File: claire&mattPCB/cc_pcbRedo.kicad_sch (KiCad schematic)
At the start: 91 parts, among them J1 Conn_02x05_Odd_Even, J2 Micro_SD_Card_Det_Hirose_DM3AT, J3 4x4 Keypad, J4 DC-DC_JUMPER, J5 PS_WIRES, J6 PS_BJ, J7 DC-DC Converter, SW1 SW_Push, U1 ESP8266, U2 7in_display_controller, U3 RFID_Scanner, U4 TFT_2.8IN_DISPLAY, U5 74HC14, U6 STM32F091RCTx, U7 MEZD71201AF, U8 TPS56325x, U9 4N28

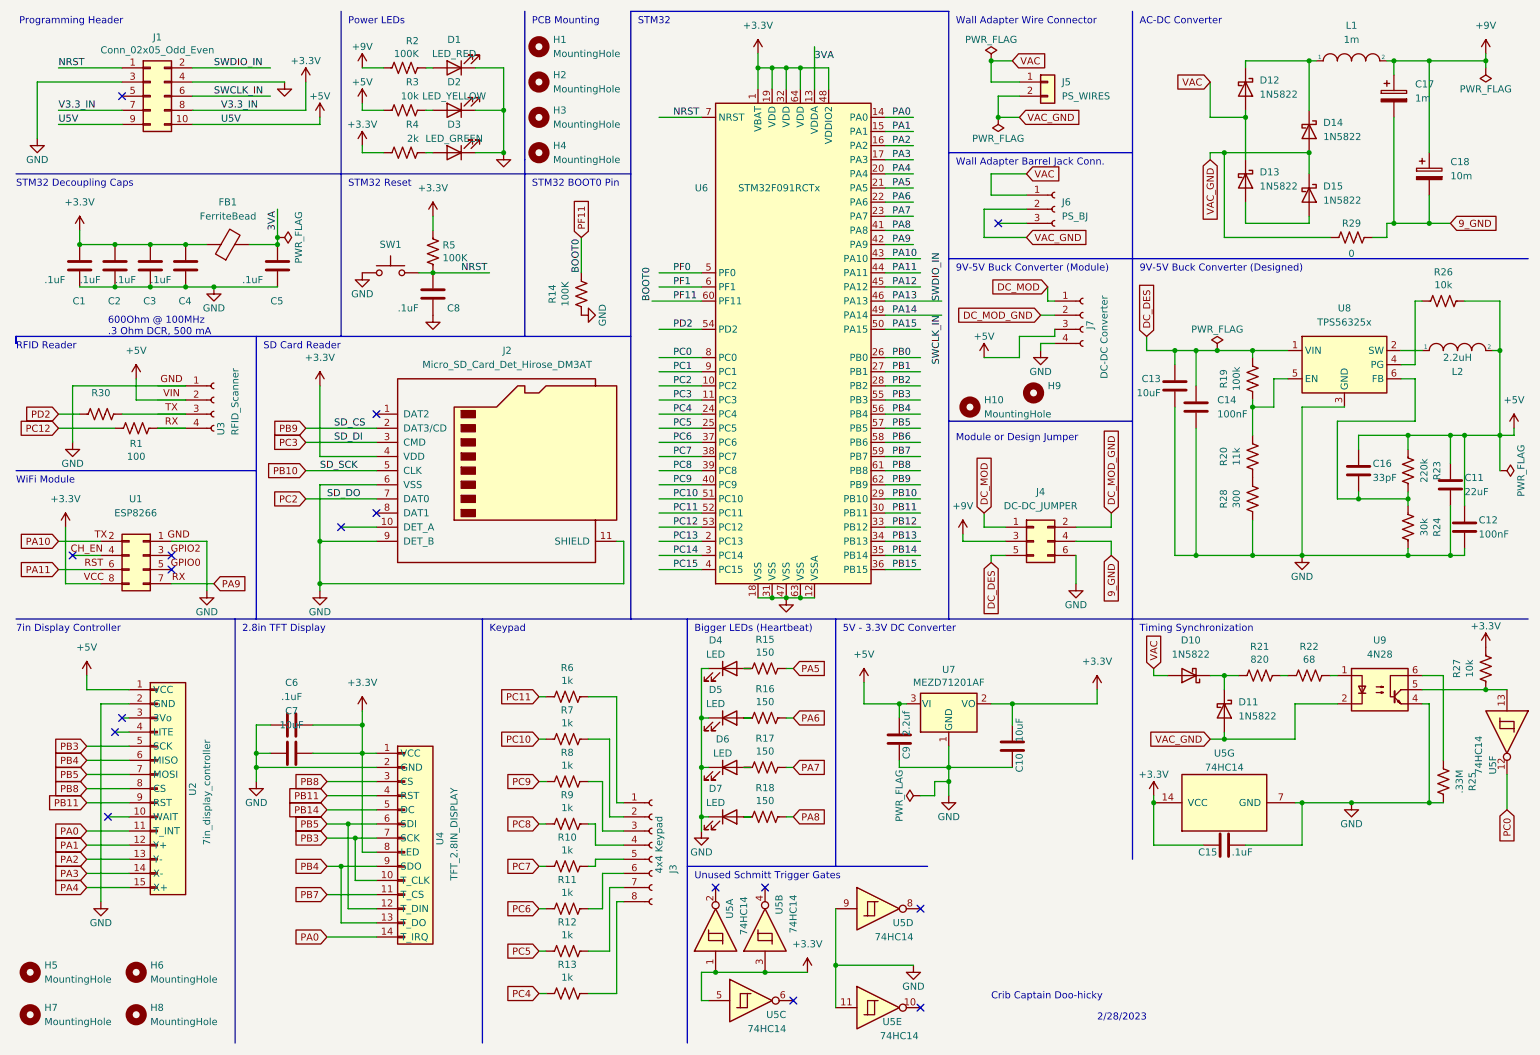
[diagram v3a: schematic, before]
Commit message: added oscillator for micro
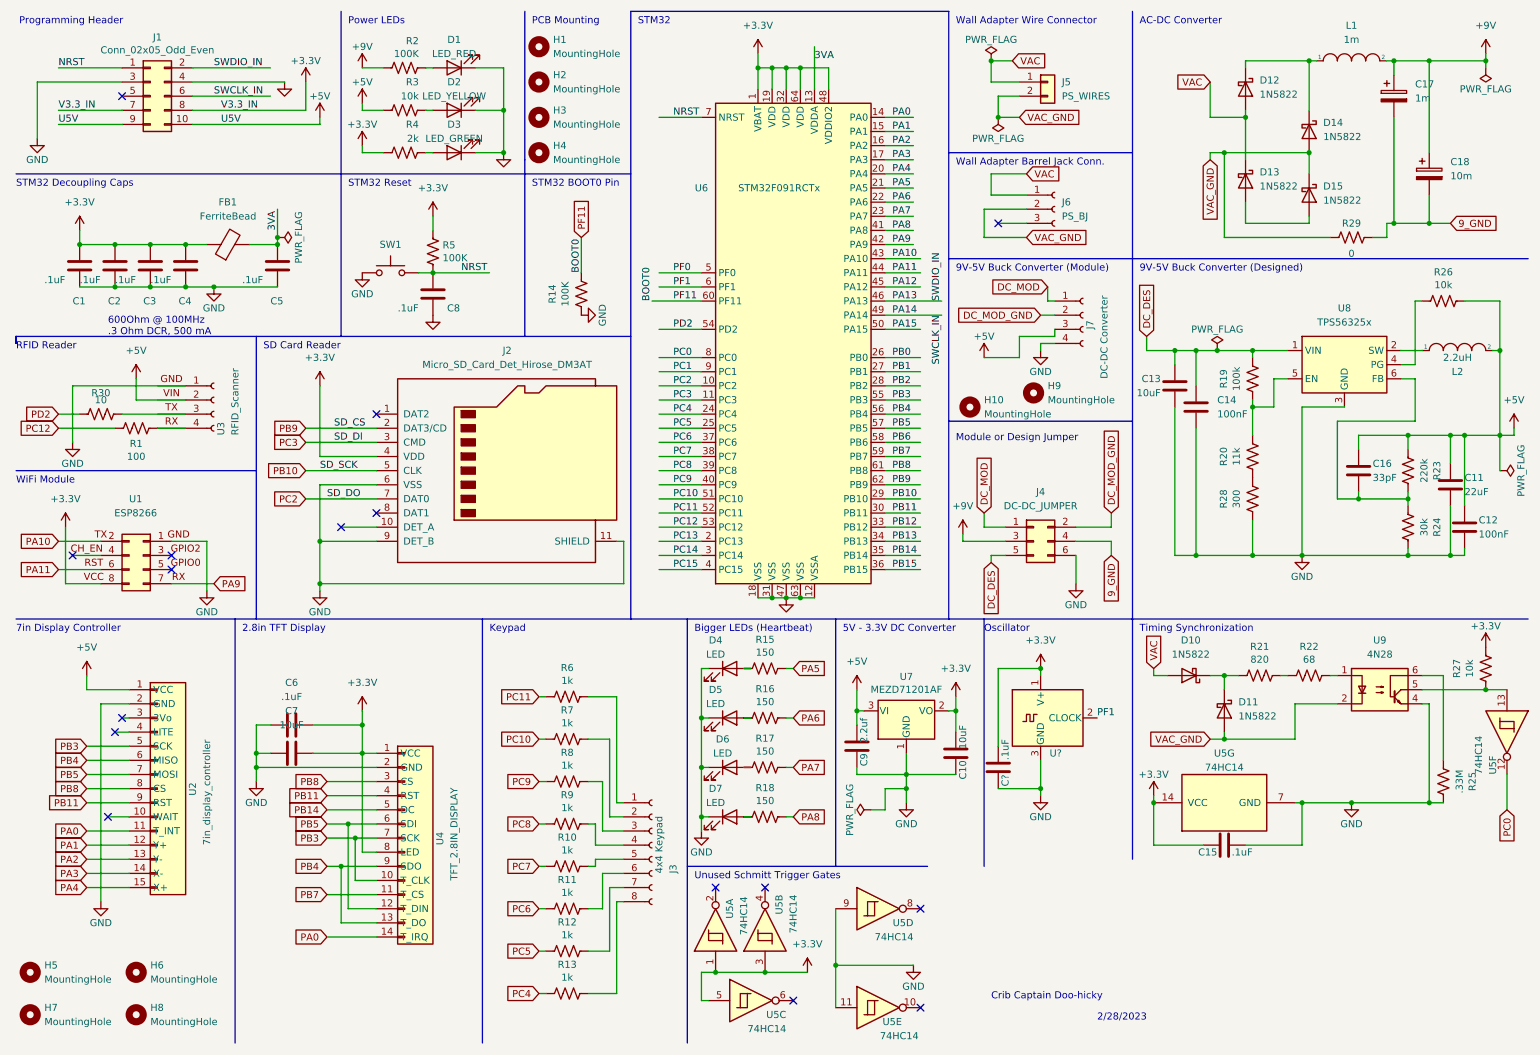
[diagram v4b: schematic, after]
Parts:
- added C?: .1uF, Capacitor_SMD:C_0805_2012Metric_Pad1.18x1.45mm_HandSolder, symbol Device:C
- added U?: (no value), symbol Oscillator:MAX7375AXR805
- H9: value (none) -> MountingHole; footprint (none) -> imported_footprints:MountingHole_2.2mm
- R30: value (none) -> 10
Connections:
- net +3V3: now also C?.2, U?.1 (V+)
- net GND: now also C?.1, U?.3 (GND)
- net PF1: now also U?.2 (CLOCK)
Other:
- note added: "Oscillator"
- moved on the sheet: C10, C9, U7

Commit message: added diodes pointing to where 5V outputs
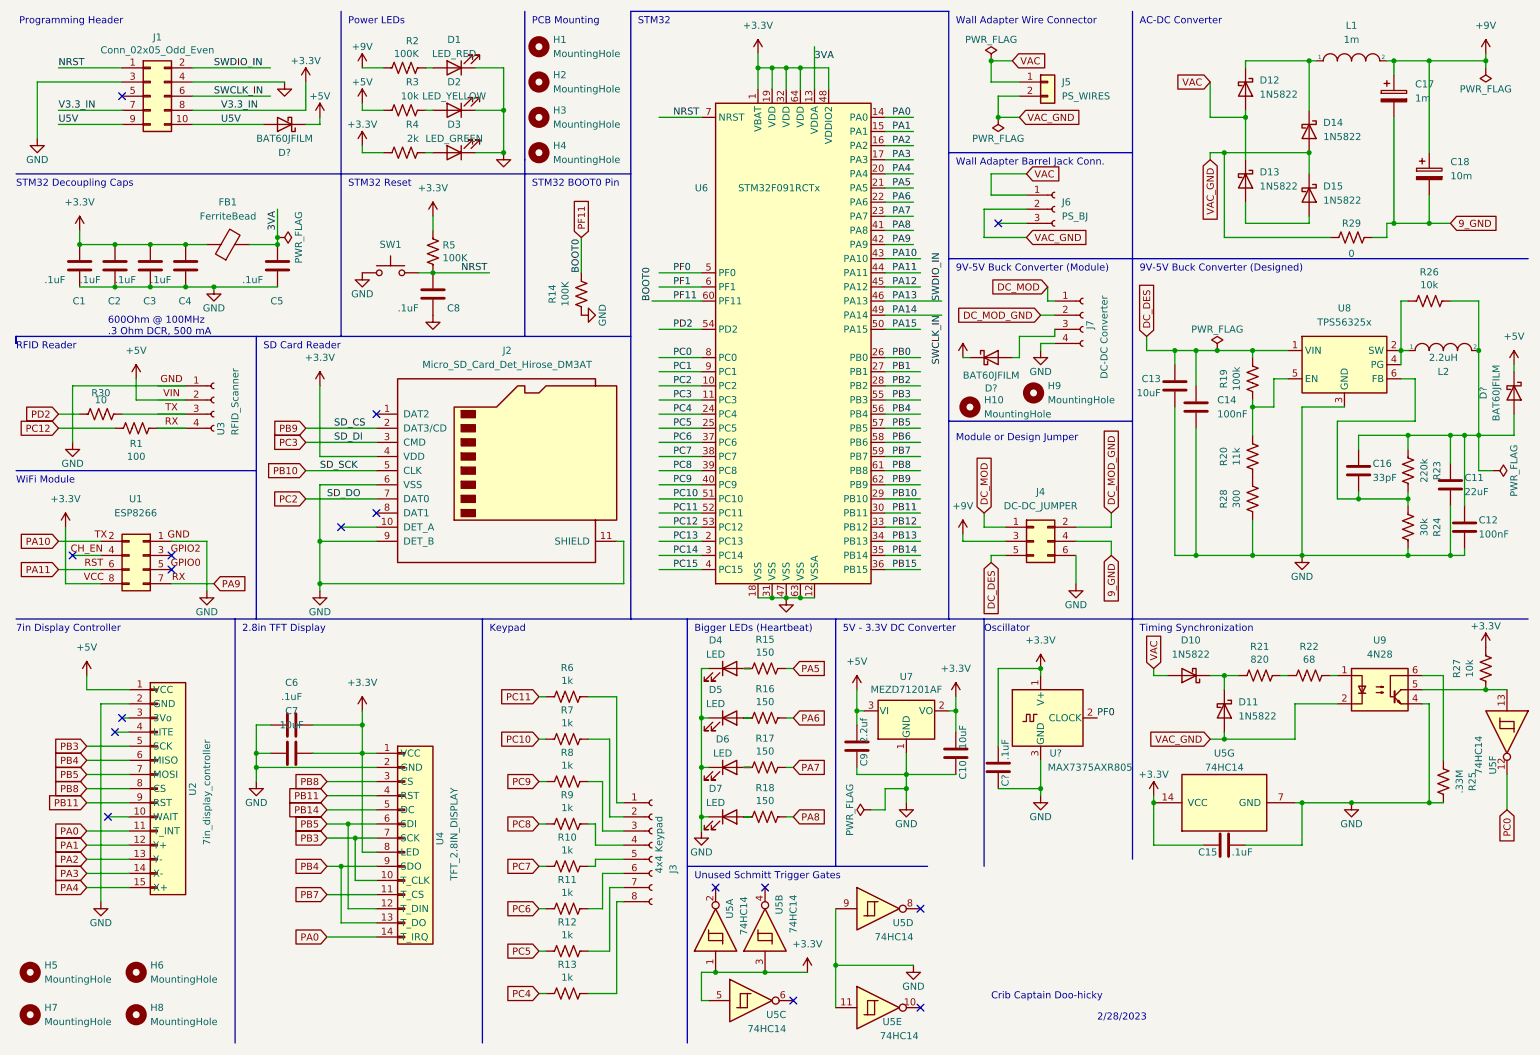
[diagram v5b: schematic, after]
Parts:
- added D? (x3): BAT60JFILM, Diode_SMD:D_SOD-323, symbol Diode:BAT60A
- U?: value (none) -> MAX7375AXR805; footprint (none) -> Package_TO_SOT_SMD:SOT-323_SC-70
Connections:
- net +5V: now also D?.1 (K), D?.1 (K), D?.1 (K); no longer C11.1, C12.1, C16.1, J1.10 (Pin_10), J1.9 (Pin_9), J7.3 (Pin_3), L2.2, R23.2, R26.1
- net PF0: now also U?.2 (CLOCK)
- net PF1: no longer U?.2 (CLOCK)
- net at R26.2, U8.4 (PG): now also L2.1, U8.2 (SW)
- new net: C11.1, C12.1, C16.1, D?.2 (A), L2.2, R23.2, R26.1
- new net: D?.2 (A), J7.3 (Pin_3)
- new net U5V: D?.2 (A), J1.10 (Pin_10), J1.9 (Pin_9)
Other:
- moved on the sheet: L2, R26

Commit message: diodes and vias w labels added
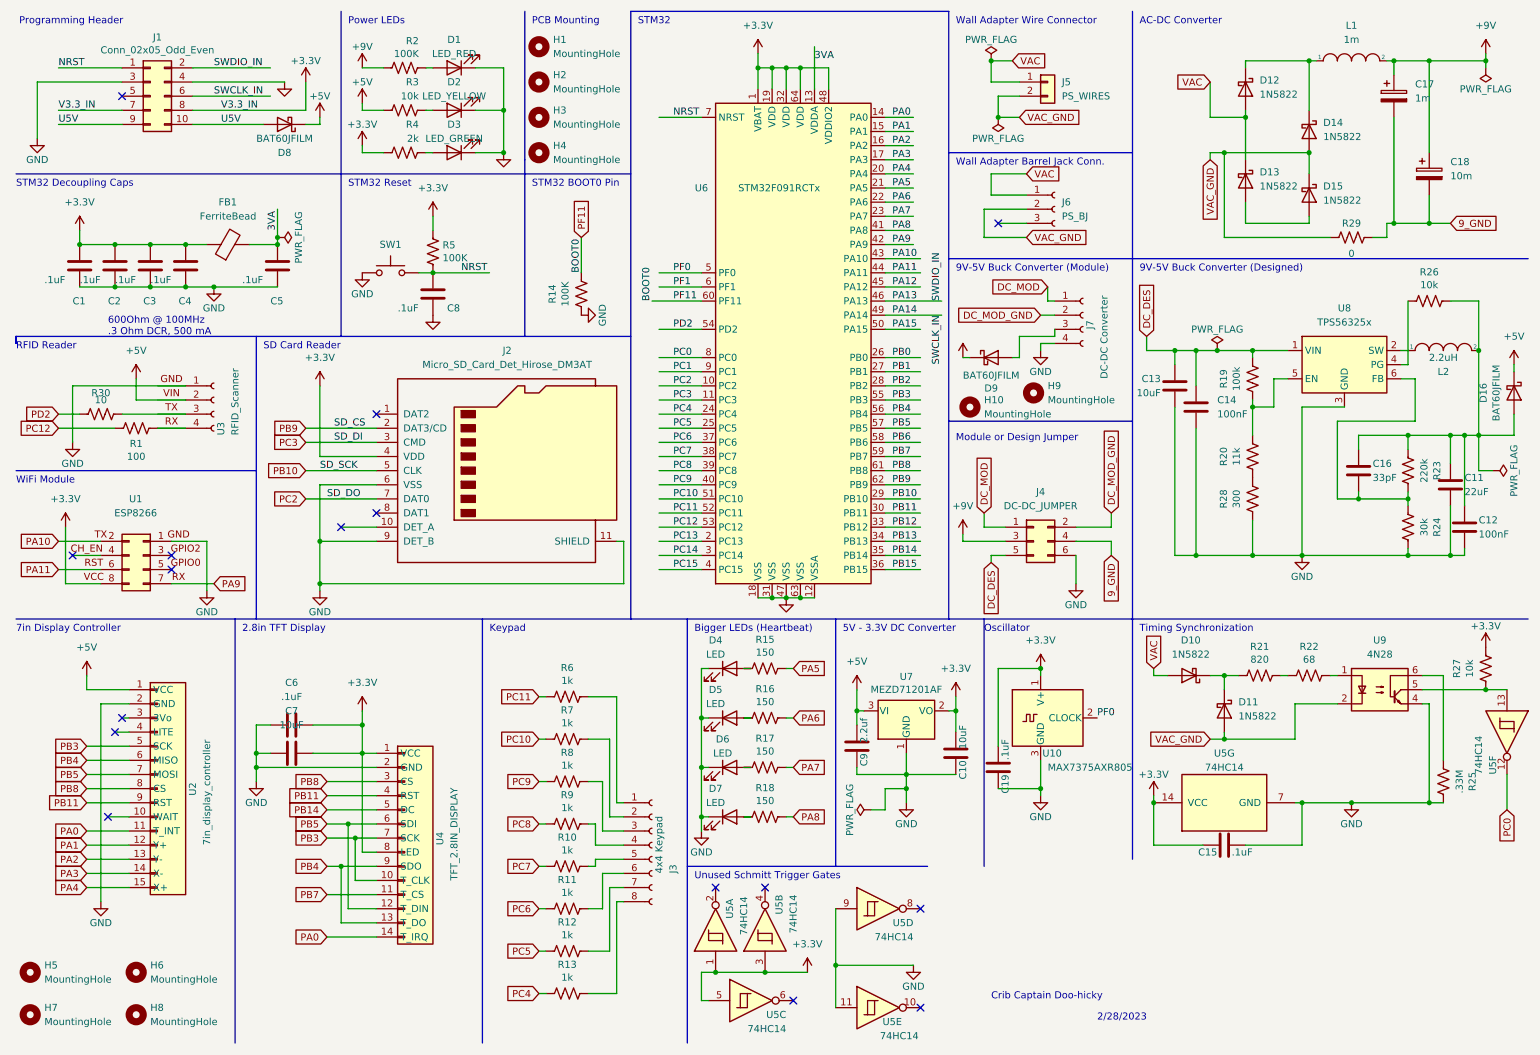
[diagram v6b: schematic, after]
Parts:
- gave numbers to parts that had none: 5
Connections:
- net at R26.2, U8.4 (PG): no longer L2.1, U8.2 (SW)
- new net: L2.1, U8.2 (SW)
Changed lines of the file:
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@@
   (junction (at 196.85 130.81) (diameter 0) (color 0 0 0 0)
   )
-  (junction (at 261.62 73.66) (diameter 0) (color 0 0 0 0)
-  )
   (junction (at 148.59 118.11) (diameter 0) (color 0 0 0 0)
   )
@@
     (stroke (width 0) (type default) (color 0 0 0 0))
   )
+  (wire (pts (xy 262.89 76.2) (xy 261.62 76.2))
+    (stroke (width 0) (type default) (color 0 0 0 0))
+  )
   (wire (pts (xy 276.86 21.59) (xy 276.86 20.32))
     (stroke (width 0) (type default) (color 0 0 0 0))
@@
     (stroke (width 0) (type default) (color 0 0 0 0))
   )
-  (wire (pts (xy 261.62 76.2) (xy 261.62 73.66))
-    (stroke (width 0) (type default) (color 0 0 0 0))
-  )
   (wire (pts (xy 144.78 130.81) (xy 143.51 130.81))
     (stroke (width 0) (type default) (color 0 0 0 0))
@@
     (stroke (width 0) (type default) (color 0 0 0 0))
   )
-  (wire (pts (xy 261.62 73.66) (xy 261.62 64.77))
-    (stroke (width 0) (type default) (color 0 0 0 0))
-  )
   (wire (pts (xy 64.77 25.4) (xy 64.77 30.48))
     (stroke (width 0) (type default) (color 0 0 0 0))
@@
     (stroke (width 0) (type default) (color 0 0 0 0))
   )
+  (wire (pts (xy 262.89 73.66) (xy 261.62 73.66))
+    (stroke (width 0) (type default) (color 0 0 0 0))
+  )
   (wire (pts (xy 266.7 50.8) (xy 266.7 45.72))
     (stroke (width 0) (type default) (color 0 0 0 0))
@@
     (stroke (width 0) (type default) (color 0 0 0 0))
   )
-  (wire (pts (xy 261.62 73.66) (xy 262.89 73.66))
-    (stroke (width 0) (type default) (color 0 0 0 0))
-  )
   (wire (pts (xy 120.65 107.95) (xy 121.92 107.95))
     (stroke (width 0) (type default) (color 0 0 0 0))
@@
     (stroke (width 0) (type default) (color 0 0 0 0))
   )
-  (wire (pts (xy 261.62 64.77) (xy 262.89 64.77))
-    (stroke (width 0) (type default) (color 0 0 0 0))
-  )
   (wire (pts (xy 68.58 179.07) (xy 77.47 179.07))
     (stroke (width 0) (type default) (color 0 0 0 0))
@@
     (stroke (width 0) (type default) (color 0 0 0 0))
   )
+  (wire (pts (xy 262.89 64.77) (xy 262.89 76.2))
+    (stroke (width 0) (type default) (color 0 0 0 0))
+  )
   (wire (pts (xy 259.08 50.8) (xy 259.08 53.34))
     (stroke (width 0) (type default) (color 0 0 0 0))
@@
   (symbol (lib_id "Oscillator:MAX7375AXR805") (at 196.85 139.7 0) (unit 1)
     (in_bom yes) (on_board yes)
-    (property "Reference" "U?" (id 0) (at 200.66 146.05 0)
+    (property "Reference" "U10" (id 0) (at 200.66 146.05 0)
       (effects (font (size 1.27 1.27)) (justify right))
     )
@@
   (symbol (lib_id "Diode:BAT60A") (at 60.96 33.02 180) (unit 1)
     (in_bom yes) (on_board yes)
-    (property "Reference" "D?" (id 0) (at 60.96 38.1 0))
+    (property "Reference" "D8" (id 0) (at 60.96 38.1 0))
     (property "Value" "BAT60JFILM" (id 1) (at 60.96 35.56 0))
     (property "Footprint" "Diode_SMD:D_SOD-323" (id 2) (at 60.96 28.575 0)
@@
   (symbol (lib_id "Diode:BAT60A") (at 281.94 81.28 270) (unit 1)
     (in_bom yes) (on_board yes)
-    (property "Reference" "D?" (id 0) (at 276.4282 81.28 0))
+    (property "Reference" "D16" (id 0) (at 276.4282 81.28 0))
     (property "Value" "BAT60JFILM" (id 1) (at 278.7396 81.28 0))
     (property "Footprint" "Diode_SMD:D_SOD-323" (id 2) (at 277.495 81.28 0)
@@
   (symbol (lib_id "power:GND") (at 196.85 153.67 0) (unit 1)
     (in_bom yes) (on_board yes)
-    (property "Reference" "#PWR?" (id 0) (at 196.85 160.02 0)
+    (property "Reference" "#PWR041" (id 0) (at 196.85 160.02 0)
       (effects (font (size 1.27 1.27)) hide)
     )
@@
   (symbol (lib_id "Diode:BAT60A") (at 187.96 74.93 0) (unit 1)
     (in_bom yes) (on_board yes)
-    (property "Reference" "D?" (id 0) (at 187.96 80.4418 0))
+    (property "Reference" "D9" (id 0) (at 187.96 80.4418 0))
     (property "Value" "BAT60JFILM" (id 1) (at 187.96 78.1304 0))
     (property "Footprint" "Diode_SMD:D_SOD-323" (id 2) (at 187.96 79.375 0)
@@
   (symbol (lib_id "power:+3.3V") (at 196.85 130.81 0) (unit 1)
     (in_bom yes) (on_board yes) (fields_autoplaced)
-    (property "Reference" "#PWR?" (id 0) (at 196.85 134.62 0)
+    (property "Reference" "#PWR06" (id 0) (at 196.85 134.62 0)
       (effects (font (size 1.27 1.27)) hide)
     )
@@
   (symbol (lib_id "Device:C") (at 189.23 148.59 180) (unit 1)
     (in_bom yes) (on_board yes)
-    (property "Reference" "C?" (id 0) (at 190.5 149.86 90)
+    (property "Reference" "C19" (id 0) (at 190.5 149.86 90)
       (effects (font (size 1.27 1.27)) (justify left))
     )
@@
       (reference "#PWR05") (unit 1) (value "GND") (footprint "")
     )
+    (path "/dd230ea3-afaa-497d-b127-d3d08290224d"
+      (reference "#PWR06") (unit 1) (value "+3.3V") (footprint "")
+    )
     (path "/a1a3d887-4b1f-43d6-8c77-762b960f3671"
       (reference "#PWR07") (unit 1) (value "GND") (footprint "")
@@
       (reference "#PWR040") (unit 1) (value "+5V") (footprint "")
     )
+    (path "/64bd04c9-cca0-4f01-8fc3-59ded04ece1a"
+      (reference "#PWR041") (unit 1) (value "GND") (footprint "")
+    )
     (path "/4dae2e8a-b111-4716-acaf-b559258f7b17"
       (reference "#PWR0101") (unit 1) (value "+3.3V") (footprint "")
@@
       (reference "#PWR0103") (unit 1) (value "+5V") (footprint "")
     )
-    (path "/64bd04c9-cca0-4f01-8fc3-59ded04ece1a"
-      (reference "#PWR?") (unit 1) (value "GND") (footprint "")
-    )
-    (path "/dd230ea3-afaa-497d-b127-d3d08290224d"
-      (reference "#PWR?") (unit 1) (value "+3.3V") (footprint "")
-    )
     (path "/1075c308-b5bb-44bc-847a-178364e5c8cd"
       (reference "C1") (unit 1) (value ".1uF") (footprint "Capacitor_SMD:C_0805_2012Metric_Pad1.18x1.45mm_HandSolder")
@@
     )
     (path "/fd385b2e-f50d-4299-8bf4-3ec14af15bf7"
-      (reference "C?") (unit 1) (value ".1uF") (footprint "Capacitor_SMD:C_0805_2012Metric_Pad1.18x1.45mm_HandSolder")
+      (reference "C19") (unit 1) (value ".1uF") (footprint "Capacitor_SMD:C_0805_2012Metric_Pad1.18x1.45mm_HandSolder")
     )
     (path "/8ca397b9-b092-4926-83dc-ea9a3b15efd9"
@@
       (reference "D7") (unit 1) (value "LED") (footprint "LED_THT:LED_D3.0mm")
     )
+    (path "/268f5414-0857-446e-aa2a-7444983f16f0"
+      (reference "D8") (unit 1) (value "BAT60JFILM") (footprint "Diode_SMD:D_SOD-323")
+    )
+    (path "/731a70de-1642-4be5-b5a9-2acbaf7fbc3b"
+      (reference "D9") (unit 1) (value "BAT60JFILM") (footprint "Diode_SMD:D_SOD-323")
+    )
     (path "/cf6f8618-d325-410e-b4b2-66285b39f3df"
       (reference "D10") (unit 1) (value "1N5822") (footprint "imported_footprints:DIO_1N5822")
@@
       (reference "D15") (unit 1) (value "1N5822") (footprint "imported_footprints:DIO_1N5822")
     )
-    (path "/268f5414-0857-446e-aa2a-7444983f16f0"
-      (reference "D?") (unit 1) (value "BAT60JFILM") (footprint "Diode_SMD:D_SOD-323")
-    )
     (path "/4c9375c0-f2a2-4e4e-bd4b-b8968bc40be2"
-      (reference "D?") (unit 1) (value "BAT60JFILM") (footprint "Diode_SMD:D_SOD-323")
-    )
-    (path "/731a70de-1642-4be5-b5a9-2acbaf7fbc3b"
-      (reference "D?") (unit 1) (value "BAT60JFILM") (footprint "Diode_SMD:D_SOD-323")
+      (reference "D16") (unit 1) (value "BAT60JFILM") (footprint "Diode_SMD:D_SOD-323")
     )
     (path "/c8ff2f12-4068-40f4-bc3e-bebece6677d1"
@@
     )
     (path "/1dc09ae3-020f-422e-ad6c-2ebcd029e1de"
-      (reference "U?") (unit 1) (value "MAX7375AXR805") (footprint "Package_TO_SOT_SMD:SOT-323_SC-70")
+      (reference "U10") (unit 1) (value "MAX7375AXR805") (footprint "Package_TO_SOT_SMD:SOT-323_SC-70")
     )
   )
